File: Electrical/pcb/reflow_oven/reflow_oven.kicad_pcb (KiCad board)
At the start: 2 copper layers, 146.1 x 134.4 mm, 249 parts, among them J1 1711738, J10 THC IN, J11 THC IN, J12 NTC_A IN, J13 NTC_B IN, J14 3V3 out, J15 5V out, J16 SSR_A, J17 FAN power in, J18 FAN out, J19 SSR_B, J2 Conn_01x06, J3 USER BOARD DISPLAY, J4 USER BOARD BUTTON, J5 DB9_Female_MountingHoles, J6 Line IN, J7 Heater_A, J8 Line IN, J9 Heater_B, P1 USB_C_Receptacle_USB2.0, Q1 DMN13H750S, Q2 AO3402, Q3 DMN13H750S, SW1 SW_MEC_5E, T1 ZMPT101B, T2 ZMPT101B, U1 LH05-10B05, U10 TLP2361, U11 COS6001, U12 COS6001, U13 COS6001, U14 COS6001, U2 AP1117-33, U3 STM32F030CCTx, U4 CP2102N-Axx-xQFN28, U5 MAX485E, U6 MAX6675ISA+T, U7 MAX6675ISA+T, U8 ACS758LCB-050B-PFF, U9 ACS758LCB-050B-PFF, Y1 8MHz 8pF

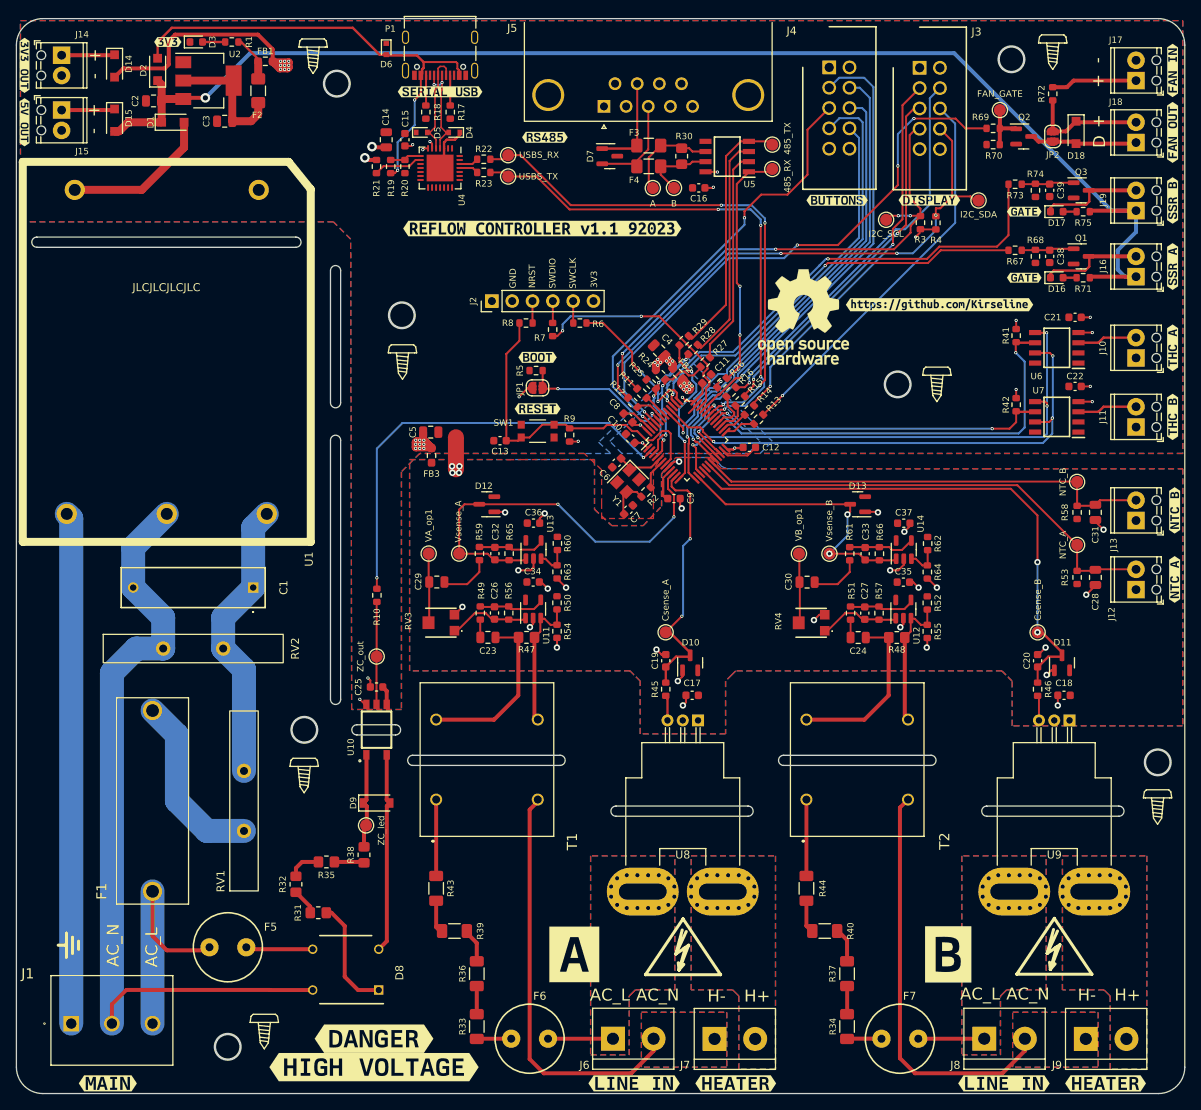
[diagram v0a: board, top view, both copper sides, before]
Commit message: addon
documentation pics
adjust oshw logo
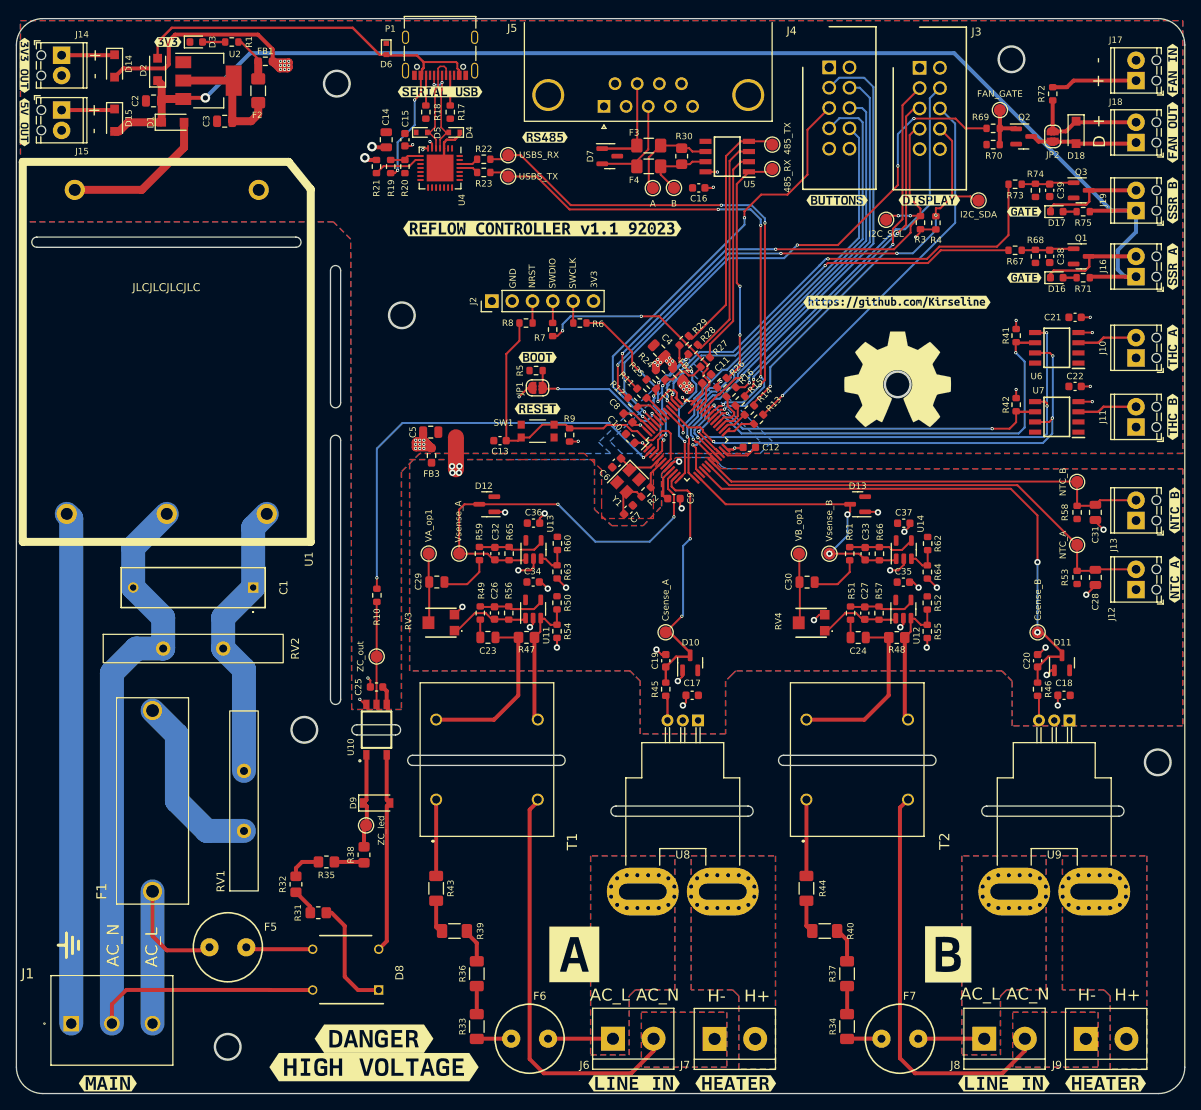
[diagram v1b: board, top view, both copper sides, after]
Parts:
- removed the REF** at (267.6, 91.0)
- removed the REF** at (186.4, 129.7)
- removed the REF** at (221.4, 204.7)
- removed the REF** at (169.1, 213.4)
- removed the REF** at (267.8, 204.6)
- removed the REF** at (174.1, 181.4)
- removed the REF** at (236.5, 125.2)
- removed the REF** at (280.7, 185.3)
- removed the REF** at (253.2, 132.5)
- removed the REF** at (175.2, 91.5)
- added REF**: OSHW-Symbol_13.4x12mm_SilkScreen, Symbol:OSHW-Symbol_13.4x12mm_SilkScreen, F.Cu at (248.2, 133.0)
- D14, D15, D18: value DSS34 -> BAS85
- F5: value Fuse -> 250mA
- moved kibuzzard-64E62C67 5.34 mm to (248.2, 123.4)
